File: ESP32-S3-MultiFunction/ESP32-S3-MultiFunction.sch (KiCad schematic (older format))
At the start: 7 parts

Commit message: WROOM module Version.
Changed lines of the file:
@@
 LIBS:ESP32-S3-MultiFunction-rescue
 LIBS:USBLC6-2SC6
+LIBS:esp32_s3_wroom
 EELAYER 25 0
 EELAYER END
@@
 F10 "GPIO38(Buttons1)" I R 7750 3500 60
 F11 "GPIO9(Motor1)" O R 7750 2250 60
-F12 "GPIO34(OD1)" I L 3900 3700 60
+F12 "GPIO40(OD1)" I L 3900 3700 60
 F13 "GPIO35(OD2)" I L 3900 3800 60
 F14 "GPIO36(OD3)" I L 3900 3900 60
 F15 "GPIO7(OD4)" I L 3900 4000 60
 F16 "GPIO8(Motor3)" O R 7750 2450 60
-F17 "GPIO33(Motor4)" O R 7750 2550 60
+F17 "GPIO39(Motor4)" O R 7750 2550 60
 F18 "GPIO12(Points1)" I R 7750 2700 60
 F19 "GPIO13(Points2)" I R 7750 2800 60

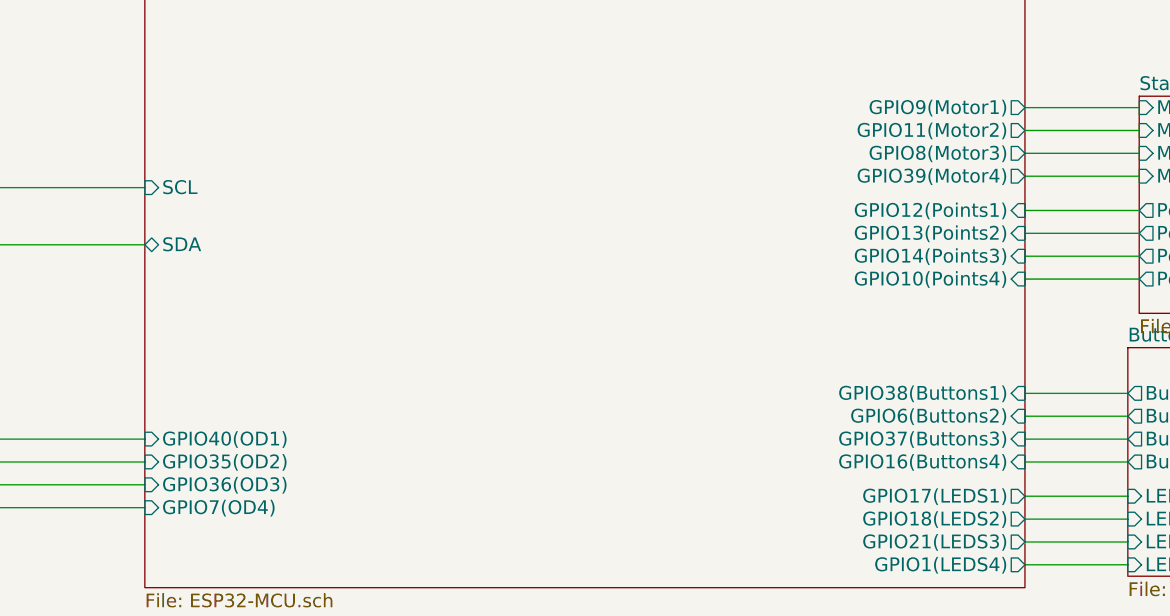
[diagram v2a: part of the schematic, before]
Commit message: Revert to chip version, USB-C, replace reset and boot buttons.
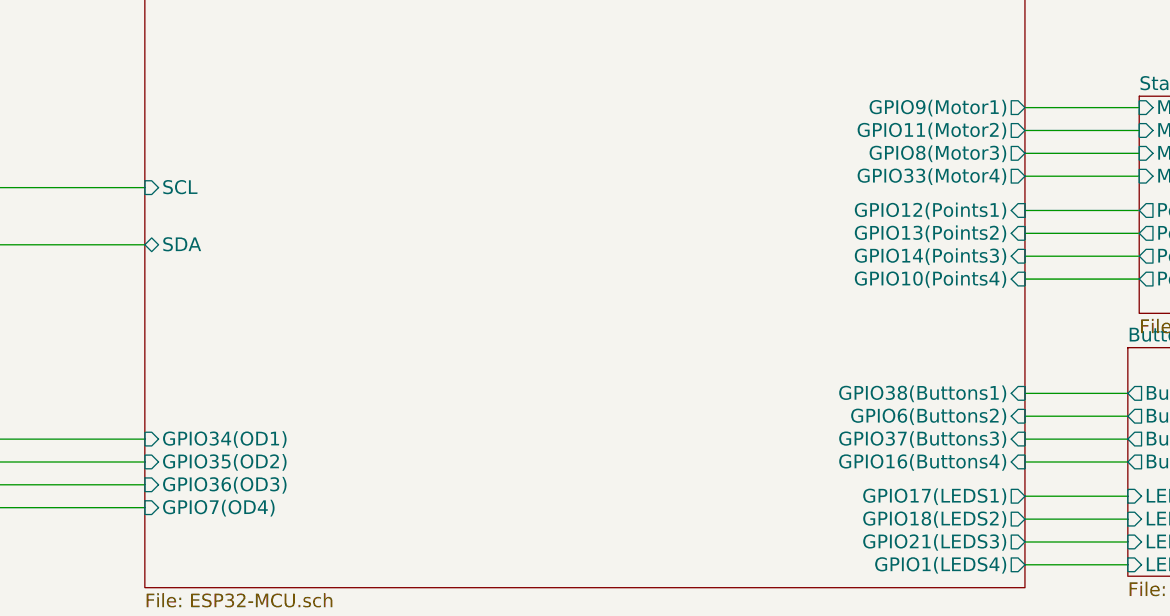
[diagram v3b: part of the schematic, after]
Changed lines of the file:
@@
 F10 "GPIO38(Buttons1)" I R 7750 3500 60
 F11 "GPIO9(Motor1)" O R 7750 2250 60
-F12 "GPIO40(OD1)" I L 3900 3700 60
+F12 "GPIO34(OD1)" I L 3900 3700 60
 F13 "GPIO35(OD2)" I L 3900 3800 60
 F14 "GPIO36(OD3)" I L 3900 3900 60
 F15 "GPIO7(OD4)" I L 3900 4000 60
 F16 "GPIO8(Motor3)" O R 7750 2450 60
-F17 "GPIO39(Motor4)" O R 7750 2550 60
+F17 "GPIO33(Motor4)" O R 7750 2550 60
 F18 "GPIO12(Points1)" I R 7750 2700 60
 F19 "GPIO13(Points2)" I R 7750 2800 60
